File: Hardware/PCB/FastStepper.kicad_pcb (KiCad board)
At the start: 4 copper layers, 61.9 x 84.4 mm, 138 parts, among them IC1 FT232RL, IC10 THS4281DBVT, IC11 M74VHC1GT126DT1G, IC13 M74VHC1GT126DT1G, IC14 M74VHC1GT126DT1G, IC15 M74VHC1GT126DT1G, IC16 M74VHC1GT126DT1G, IC17 M74VHC1GT126DT1G, IC18 M74VHC1GT126DT1G, IC19 M74VHC1GT126DT1G, IC2 M74VHC1GT126DT1G, IC20 M74VHC1GT126DT1G, IC21 M74VHC1GT126DT1G, IC22 M74VHC1GT126DT1G, IC3 LP5907MFX-3.3, IC4 M74VHC1GT126DT1G, IC5 M74VHC1GT126DT1G, IC6 M74VHC1GT126DT1G, IC8 ATXMEGA32A4U, J1 USB_C_Receptacle, J2 PJ-316A-6A, J3 PJ-316A-6A, J4 Keystone 8734, J6 Keystone 8734, Q1 AO3401A, U1 74LVC1G157, U2 THVD1450D, U3 ADUM1201BRZ, X1 conn 1x5 2, X10 conn 1x3, X2 conn 1x5, X3 conn 1x3, X4 conn 1x3, X5 conn 1x5, X6 OSCILLATOR, X9 conn 1x5

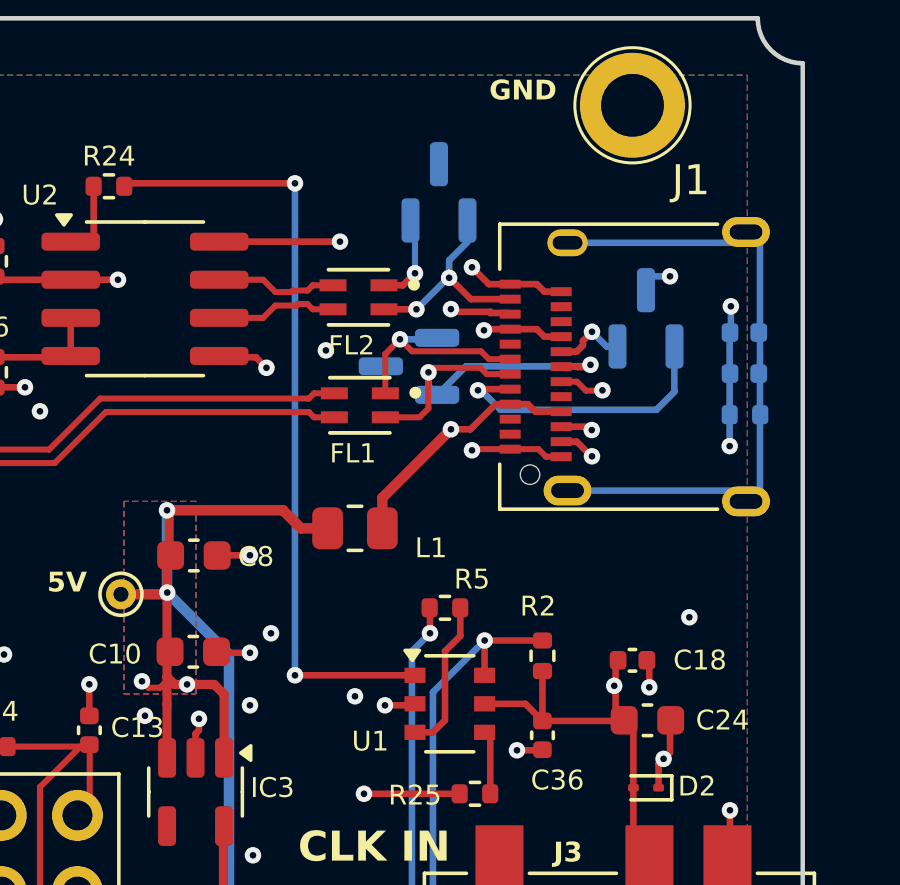
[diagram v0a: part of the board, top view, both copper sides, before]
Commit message: 1º commit com v.1.1 corrigida
	. fich USB-C; pinos B10 & B11 trocados
	. Rs de PDown nos rails USB CC1 & CC2
	. rail de VClck deixa de existir: VClck = +3V3
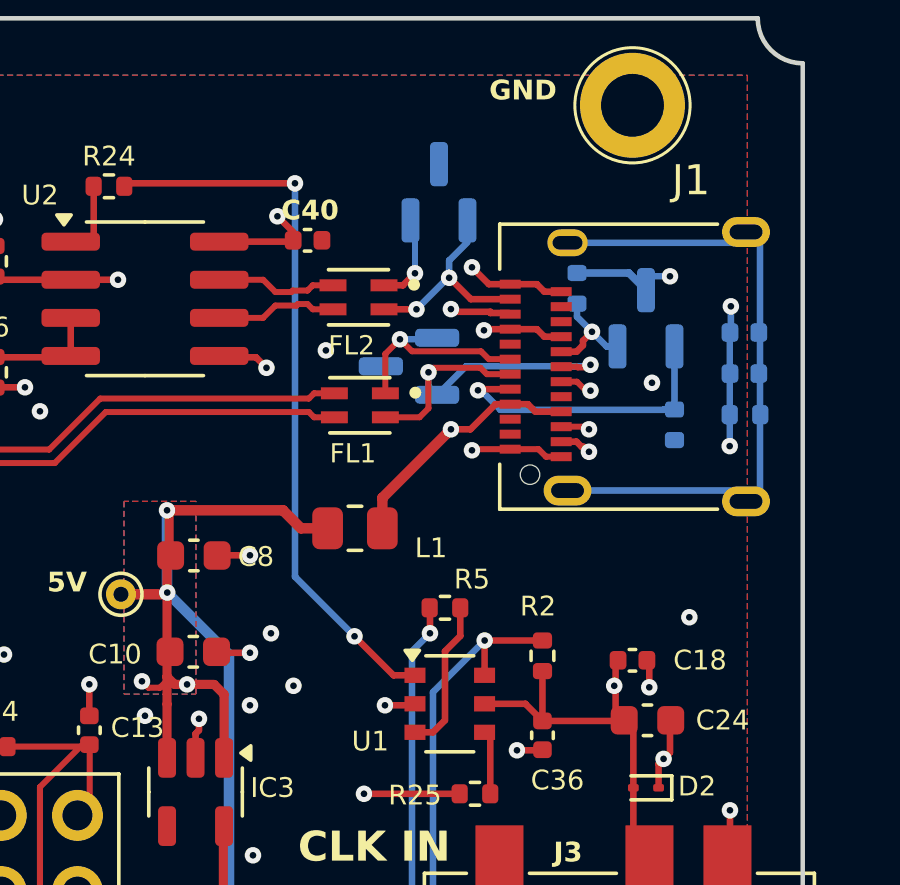
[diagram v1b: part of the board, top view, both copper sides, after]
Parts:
- added C40: 100nF, Capacitor_SMD:C_0402_1005Metric, F.Cu at (164.9, 72.0)
- added R28: tbd, Resistor_SMD:R_0402_1005Metric, B.Cu at (177.2, 78.2)
- added R29: tbd, Resistor_SMD:R_0402_1005Metric, B.Cu at (173.9, 73.6)
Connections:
- C18 pad 2: VClk -> +3V3
- C24 pad 1: VClk -> +3V3
- C3 pad 2: VClk -> +3V3
- C36 pad 2: VClk -> +3V3
- D2 pad 2: VClk -> +3V3
- J1 pad B10: /USB_CLCK_P -> /USB_CLCK_N
- J1 pad B11: /USB_CLCK_N -> /USB_CLCK_P
- J3 pad 3: VClk -> +3V3
- Q1 pad 2: VClk -> +3V3
- R2 pad 1: VClk -> +3V3
- U1 pad 5: VClk -> +3V3
- U2 pad 8: VClk -> +3V3
- U3 pad 1: VClk -> +3V3
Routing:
- net +3V3: track 299.1 -> 390.4 mm, vias 21 -> 24
- net VClk: track 76.0 -> 0.00 mm, vias 3 -> 0
- net /USB_CLCK_P: track 16.4 -> 20.0 mm
- net GND: track 104.6 -> 107.1 mm, vias 160 -> 161
- net CLK_USB: track 26.0 -> 24.1 mm
- net /USB_CLCK_N: track 16.6 -> 18.0 mm
- net /CC2: track 2.46 -> 3.74 mm
- net /USB_N: track 16.2 -> 15.4 mm
